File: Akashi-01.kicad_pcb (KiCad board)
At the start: 2 copper layers, 71.1 x 67.3 mm, 33 parts, among them CN10 Conn_02x19_Odd_Even, CN7 Conn_02x19_Odd_Even, SW1 Rotary_Encoder_Switch

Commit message: Change the copy right size.
From 1.0 to 1.5

Issue : Copyright is too small #2
https://github.com/suikan4github/Akashi-01/issues/2
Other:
- board text added: "Akashi-01 v1.0.1 A Murasaki JIG for Nucleo 64 (C) Seiichi Horie 2019 https://github.com/suikan4github/Akashi-01"
- board text removed: "Akashi-01 A Murasaki JIG for Nucleo 64 (C) Seiichi Horie 2019 https://github.com/suikan4github/Akashi-01"
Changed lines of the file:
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@@
     (effects (font (size 1 1) (thickness 0.15)))
   )
-  (gr_text "Akashi-01\nA Murasaki JIG for Nucleo 64\n(C) Seiichi Horie 2019\nhttps://github.com/suikan4github/Akashi-01" (at 168.91 60.96) (layer B.SilkS)
-    (effects (font (size 1 1) (thickness 0.15)) (justify left mirror))
+  (gr_text "Akashi-01 v1.0.1\nA Murasaki JIG for Nucleo 64\n(C) Seiichi Horie 2019\nhttps://github.com/suikan4github/Akashi-01" (at 175.895 60.96) (layer B.SilkS)
+    (effects (font (size 1.5 1.5) (thickness 0.15)) (justify left mirror))
   )
   (dimension 71.12 (width 0.15) (layer Dwgs.User)

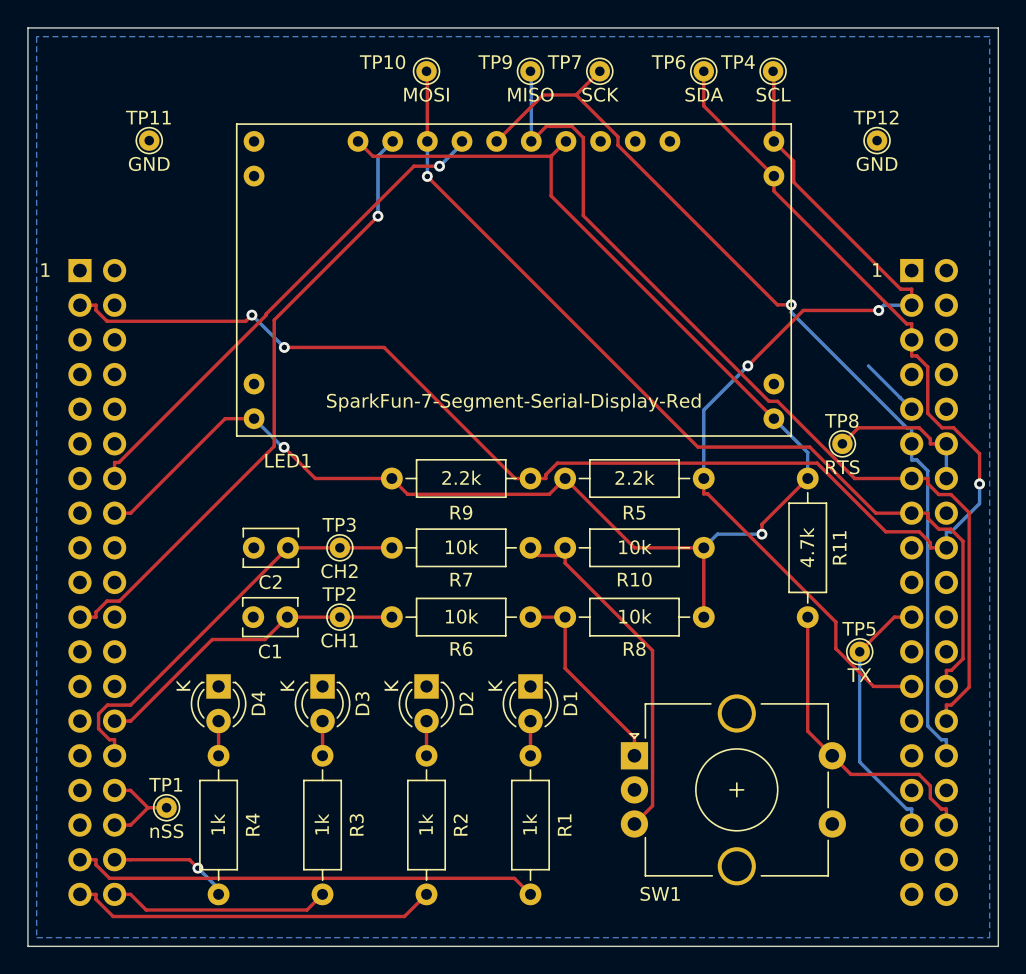
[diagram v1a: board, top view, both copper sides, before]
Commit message: Change test point drill size.
Issue 1 : Test point hole is too small #1
https://github.com/suikan4github/Akashi-01/issues/1
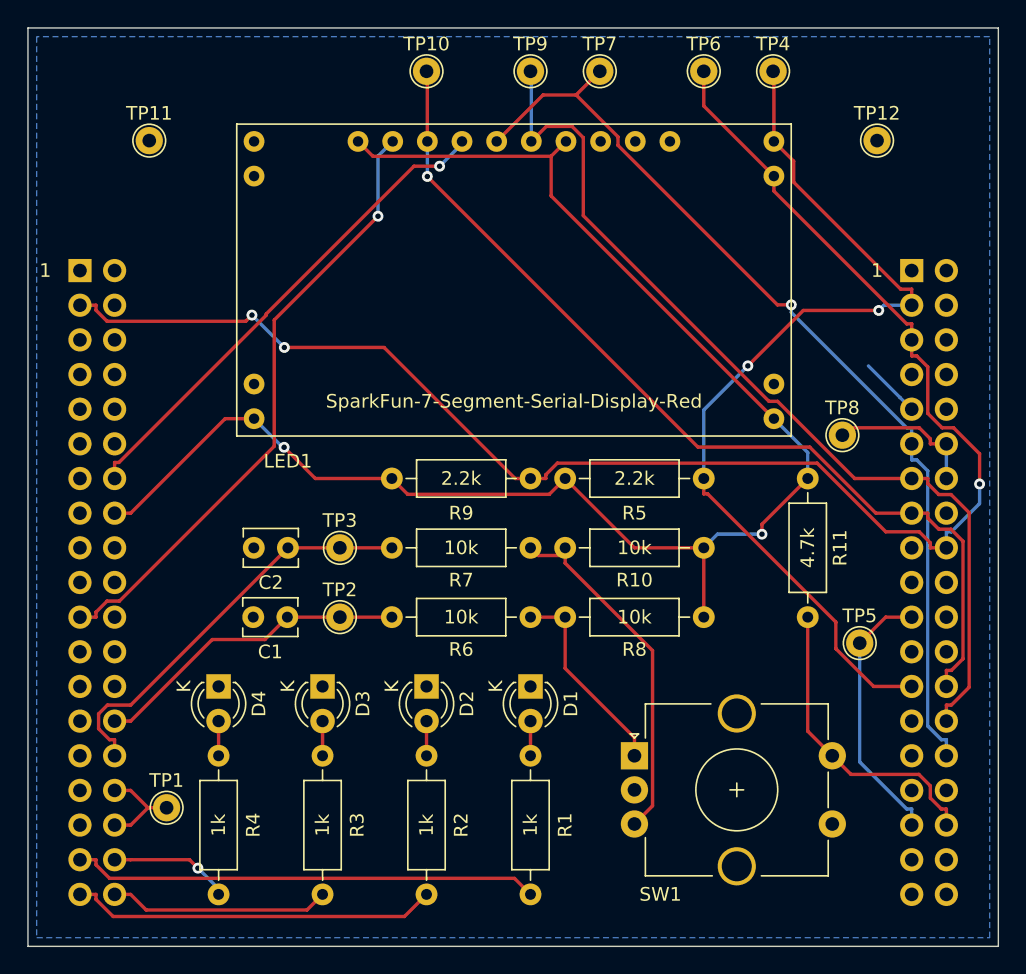
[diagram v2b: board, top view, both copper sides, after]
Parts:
- CN10, CN7: value Conn_02x19_Odd_Even -> PPPC192LFBN-RC
- SW1: value Rotary_Encoder_Switch -> PEC11R-4220F-S0024
- TP1, TP10, TP11, TP12, TP2, TP3, TP4, TP5, TP6, TP7, TP8, TP9: footprint TestPoint:TestPoint_THTPad_D1.5mm_Drill0.7mm -> TestPoint:TestPoint_THTPad_D2.0mm_Drill1.0mm
- moved TP5 0.64 mm to (176.5, 88.3)
- moved TP8 0.63 mm to (175.3, 73.0)
